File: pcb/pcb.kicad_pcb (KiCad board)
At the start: 2 copper layers, 130.9 x 223.4 mm, 38 parts, among them J1 Conn_01x04_Pin, J2 Conn_01x06_Pin, U1 XIAO-ESP32-C5-DIP, U10 XIAO-ESP32-C5-DIP, U11 XIAO-ESP32-C5-DIP, U12 XIAO-ESP32-C5-DIP, U13 XIAO-ESP32-C5-DIP, U14 XIAO-ESP32-C5-DIP, U15 XIAO-ESP32-C5-DIP, U18 XIAO-ESP32-C5-DIP, U19 LD1117V33, U2 XIAO-ESP32-C5-DIP, U3 XIAO-ESP32-C5-DIP, U4 XIAO-ESP32-C5-DIP, U5 XIAO-ESP32-C5-DIP, U6 XIAO-ESP32-C5-DIP, U7 XIAO-ESP32-C5-DIP, U8 XIAO-ESP32-C5-DIP, U9 XIAO-ESP32-C5-DIP

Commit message: add capacitors to i/o of LD1117
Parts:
- added C1: 100nF, Capacitor_THT:C_Disc_D5.0mm_W2.5mm_P2.50mm, F.Cu at (59.5, 23.0)
- added C2: 10uF, Capacitor_THT:C_Disc_D5.0mm_W2.5mm_P2.50mm, F.Cu at (75.0, 32.0)
- moved U19 7.52 mm to (66.5, 35.1)
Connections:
- U19 pad 2: Net-(J2-Pin_6) -> Net-(U19-VO)
- U19 pad 3: +5V -> Net-(U19-VI)

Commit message: Added net classes and colors, squared away controller footprint, sorted power input battery symbol
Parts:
- U17: renamed from U16; value ~ -> ESP32-S3 DevKitC-1
- renumbered U18 to U15, U15 to U16, U19 to U18
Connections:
- net Net-(U1-GPIO25_D2) renamed /CS 1
- net Net-(U10-GPIO25_D2) renamed /CS 10
- net Net-(U11-GPIO25_D2) renamed /CS 11
- net Net-(U12-GPIO25_D2) renamed /CS 12
- net Net-(U13-GPIO25_D2) renamed /CS 13
- net Net-(U14-GPIO25_D2) renamed /CS 14
- net Net-(U15-GPIO25_D2) renamed /CS 16
- net Net-(U16-GPIO14) renamed /CS 15
- net Net-(U16-GPIO15) renamed /CS 5
- net Net-(U16-GPIO18) renamed /CS 6
- net Net-(U16-GPIO2) renamed /CS 9
- net Net-(U16-GPIO5) renamed /CS 2
- net Net-(U16-GPIO6) renamed /CS 3
- net Net-(U16-GPIO7) renamed /CS 4
- net Net-(U16-GPIO8) renamed /CS 7
- net Net-(U16-GPIO9) renamed /CS 8

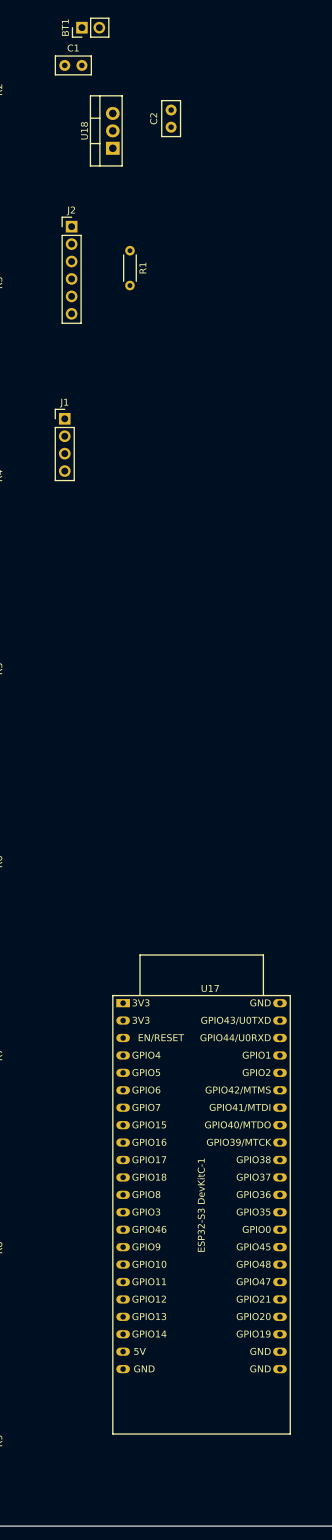
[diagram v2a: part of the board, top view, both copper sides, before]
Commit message: Fix ERC warnings, place new components in PCB
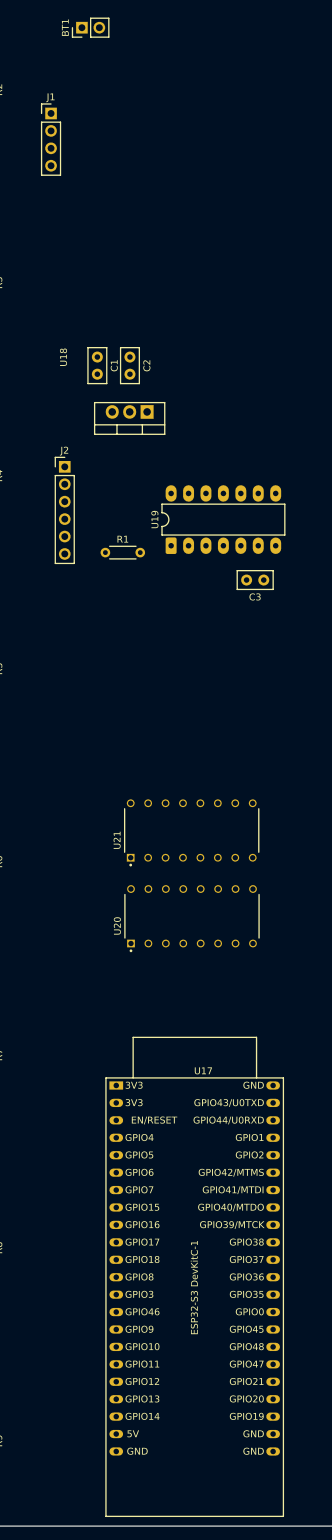
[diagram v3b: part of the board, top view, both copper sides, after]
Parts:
- added C3: 100nF, Capacitor_THT:C_Disc_D5.0mm_W2.5mm_P2.50mm, F.Cu at (88.5, 98.0)
- added U19: SN74HC125N, Package_DIP:DIP-14_W7.62mm_LongPads, F.Cu at (75.0, 93.0)
- added U20: SN74HC138N, SN74HC138N:DIP794W45P254L1969H508Q16, F.Cu at (78.0, 147.0)
- added U21: SN74HC138N, SN74HC138N:DIP794W45P254L1969H508Q16, F.Cu at (78.0, 134.5)
- J1: value Conn_01x04_Pin -> GPS Module Breakout
- J2: value Conn_01x06_Pin -> MicroSD Card Breakout
- moved J1 44.5 mm to (57.5, 30.0)
- moved R1 44.1 mm to (65.4, 94.0), turned to 0 degrees
- moved C1 42.8 mm to (64.2, 65.5), turned to -90 degrees
- moved U18 38.7 mm to (71.5, 73.5), turned to 180 degrees
- moved J2 35.0 mm to (59.5, 81.5)
- moved C2 34.0 mm to (69.0, 65.5), turned to -90 degrees
- moved U17 12.0 mm to (67.0, 171.7)
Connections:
- C1 pad 1: Net-(U18-VI) -> GND
- C2 pad 1: Net-(J2-Pin_6) -> /CS 00
- J2 pad 2: /SCK -> Net-(J2-Pin_2)
- J2 pad 3: /MOSI -> Net-(J2-Pin_3)
- J2 pad 4: /MISO -> Net-(J2-Pin_4)
- J2 pad 6: Net-(J2-Pin_6) -> /CS 00
- R1 pad 1: Net-(J2-Pin_1) -> /CS 00
- R1 pad 2: Net-(J2-Pin_6) -> /CS 00
- R10 pad 2: /CS 9 -> /CS 09
- R2 pad 2: /CS 1 -> /CS 01
- R3 pad 2: /CS 2 -> /CS 02
- R4 pad 2: /CS 3 -> /CS 03
- R5 pad 2: /CS 4 -> /CS 04
- R6 pad 2: /CS 5 -> /CS 05
- R7 pad 2: /CS 6 -> /CS 06
- R8 pad 2: /CS 7 -> /CS 07
- R9 pad 2: /CS 8 -> /CS 08
- U1 pad 3: /CS 1 -> /CS 01
- U17 pad 11: /CS 6 -> /CS ENABLE
- U17 pad 12: /CS 7 -> unconnected-(U17-GPIO8-Pad12)
- U17 pad 15: /CS 8 -> unconnected-(U17-GPIO9-Pad15)
- U17 pad 16: /CS 16 -> unconnected-(U17-GPIO10-Pad16)
- U17 pad 20: /CS 15 -> unconnected-(U17-GPIO14-Pad20)
- U17 pad 26: Net-(J2-Pin_1) -> unconnected-(U17-GPIO1-Pad26)
- U17 pad 27: /CS 9 -> unconnected-(U17-GPIO2-Pad27)
- U17 pad 28: /CS 10 -> unconnected-(U17-GPIO42-Pad28)
- U17 pad 29: /CS 11 -> unconnected-(U17-GPIO41-Pad29)
- U17 pad 30: /CS 12 -> unconnected-(U17-GPIO40-Pad30)
- U17 pad 31: /CS 13 -> unconnected-(U17-GPIO39-Pad31)
- U17 pad 4: /CS 1 -> /CS 00
- U17 pad 40: /CS 14 -> unconnected-(U17-GPIO21-Pad40)
- U17 pad 5: /CS 2 -> /CS Addr 1
- U17 pad 6: /CS 3 -> /CS Addr 2
- U17 pad 7: /CS 4 -> /CS Addr 3
- U17 pad 8: /CS 5 -> /CS Bank Sel
- U18 pad 3: Net-(U18-VI) -> +5V
- U2 pad 3: /CS 2 -> /CS 02
- U3 pad 3: /CS 3 -> /CS 03
- U4 pad 3: /CS 4 -> /CS 04
- U5 pad 3: /CS 5 -> /CS 05
- U6 pad 3: /CS 6 -> /CS 06
- U7 pad 3: /CS 7 -> /CS 07
- U8 pad 3: /CS 8 -> /CS 08
- U9 pad 3: /CS 9 -> /CS 09

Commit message: tidy up
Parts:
- moved J1 35.5 mm to (58.0, 65.5)
- moved C2 32.2 mm to (73.8, 97.4), turned to 180 degrees
- moved R1 28.6 mm to (63.0, 122.5)
- moved C3 21.8 mm to (92.5, 119.4)
- moved J2 21.4 mm to (58.5, 102.9)
- moved U19 19.9 mm to (72.4, 112.7)
- moved C1 17.4 mm to (68.5, 82.4)
- moved U18 16.6 mm to (73.5, 90.0)
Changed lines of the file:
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@@
 	(footprint "Package_DIP:DIP-14_W7.62mm_LongPads"
 		(layer "F.Cu")
-		(at 75 93 90)
+		(at 72.38 112.69 90)
 		(descr "14-lead though-hole mounted DIP package, row spacing 7.62mm (300 mils), LongPads")
 		(tags "THT DIP DIL PDIP 2.54mm 7.62mm 300mil LongPads")
@@
 		)
 		(point
-			(at 82.62 89.19)
+			(at 80 108.88)
 			(size 1.27)
 			(layer "F.Fab")
@@
 	(footprint "Capacitor_THT:C_Disc_D5.0mm_W2.5mm_P2.50mm"
 		(layer "F.Cu")
-		(at 69 65.5 -90)
+		(at 73.75 97.38 180)
 		(descr "C, Disc series, Radial, pin pitch=2.50mm, diameter*width=5*2.5mm^2, Capacitor, http://cdn-reichelt.de/documents/datenblatt/B300/DS_KERKO_TC.pdf")
 		(tags "C Disc series Radial pin pitch 2.50mm diameter 5mm width 2.5mm Capacitor")
 		(property "Reference" "C2"
-			(at 1.25 -2.5 90)
+			(at 1.25 -2.5 0)
 			(layer "F.SilkS")
 			(effects
@@
 		)
 		(property "Value" "10uF"
-			(at 1.25 2.5 90)
+			(at 1.25 2.5 0)
 			(layer "F.Fab")
 			(effects
@@
 		)
 		(property "Datasheet" ""
-			(at 0 0 90)
+			(at 0 0 0)
 			(layer "F.Fab")
 			(hide yes)
@@
 		)
 		(property "Description" "Unpolarized capacitor"
-			(at 0 0 90)
+			(at 0 0 0)
 			(layer "F.Fab")
 			(hide yes)
@@
 		)
 		(property "KiLib_Generator" "capacitor/THT/other"
-			(at 0 0 90)
+			(at 0 0 0)
 			(layer "F.SilkS")
 			(hide yes)
@@
 		(duplicate_pad_numbers_are_jumpers no)
 		(fp_line
-			(start -1.37 1.37)
-			(end -1.37 -1.37)
+			(start 3.87 1.37)
+			(end -1.37 1.37)
 			(stroke
 				(width 0.12)
@@
 		)
 		(fp_line
-			(start 3.87 1.37)
-			(end -1.37 1.37)
+			(start 3.87 -1.37)
+			(end 3.87 1.37)
 			(stroke
 				(width 0.12)
@@
 		)
 		(fp_line
-			(start -1.37 -1.37)
-			(end 3.87 -1.37)
+			(start -1.37 1.37)
+			(end -1.37 -1.37)
 			(stroke
 				(width 0.12)
@@
 		)
 		(fp_line
-			(start 3.87 -1.37)
-			(end 3.87 1.37)
+			(start -1.37 -1.37)
+			(end 3.87 -1.37)
 			(stroke
 				(width 0.12)
@@
 		)
 		(fp_text user "${REFERENCE}"
-			(at 1.25 0 90)
+			(at 1.25 0 0)
 			(layer "F.Fab")
 			(effects
@@
 		)
 		(pad "1" thru_hole circle
-			(at 0 0 270)
+			(at 0 0 180)
 			(size 1.6 1.6)
 			(drill 0.8)
@@
 		)
 		(pad "2" thru_hole circle
-			(at 2.5 0 270)
+			(at 2.5 0 180)
 			(size 1.6 1.6)
 			(drill 0.8)
@@
 	(footprint "Capacitor_THT:C_Disc_D5.0mm_W2.5mm_P2.50mm"
 		(layer "F.Cu")
-		(at 64.25 65.5 -90)
+		(at 68.5 82.38 -90)
 		(descr "C, Disc series, Radial, pin pitch=2.50mm, diameter*width=5*2.5mm^2, Capacitor, http://cdn-reichelt.de/documents/datenblatt/B300/DS_KERKO_TC.pdf")
 		(tags "C Disc series Radial pin pitch 2.50mm diameter 5mm width 2.5mm Capacitor")
@@
 	(footprint "Package_TO_SOT_THT:TO-220-3_Vertical"
 		(layer "F.Cu")
-		(at 71.5 73.5 180)
+		(at 73.5 90 180)
 		(descr "TO-220-3, Vertical, RM 2.54mm, see https://www.vishay.com/docs/66542/to-220-1.pdf")
 		(tags "TO-220-3 Vertical RM 2.54mm")
 		(property "Reference" "U18"
-			(at 12.15 7.96 90)
+			(at 9 -1 90)
 			(layer "F.SilkS")
 			(effects
@@
 	(footprint "Resistor_THT:R_Axial_DIN0204_L3.6mm_D1.6mm_P5.08mm_Horizontal"
 		(layer "F.Cu")
-		(at 65.42 94)
+		(at 63 122.5)
 		(descr "Resistor, Axial_DIN0204 series, Axial, Horizontal, pin pitch=5.08mm, 0.167W, length*diameter=3.6*1.6mm^2, http://cdn-reichelt.de/documents/datenblatt/B400/1_4W%23YAG.pdf")
 		(tags "Resistor Axial_DIN0204 series Axial Horizontal pin pitch 5.08mm 0.167W length 3.6mm diameter 1.6mm")
@@
 		)
 		(property "Value" "SN74HC138N"
-			(at 11.275 10.835 90)
+			(at 0.5 11.96 90)
 			(layer "F.Fab")
 			(effects
@@
 	(footprint "Connector_PinHeader_2.54mm:PinHeader_1x06_P2.54mm_Vertical"
 		(layer "F.Cu")
-		(at 59.5 81.5)
+		(at 58.5 102.88)
 		(descr "Through hole straight pin header, 1x06, 2.54mm pitch, single row")
 		(tags "Through hole pin header THT 1x06 2.54mm single row")
@@
 	(footprint "Capacitor_THT:C_Disc_D5.0mm_W2.5mm_P2.50mm"
 		(layer "F.Cu")
-		(at 88.5 98 180)
+		(at 92.5 119.38 180)
 		(descr "C, Disc series, Radial, pin pitch=2.50mm, diameter*width=5*2.5mm^2, Capacitor, http://cdn-reichelt.de/documents/datenblatt/B300/DS_KERKO_TC.pdf")
 		(tags "C Disc series Radial pin pitch 2.50mm diameter 5mm width 2.5mm Capacitor")
@@
 		)
 		(property "Value" "SN74HC138N"
-			(at 11.275 10.835 90)
+			(at 0 12 90)
 			(layer "F.Fab")
 			(effects
@@
 	(footprint "Connector_PinHeader_2.54mm:PinHeader_1x04_P2.54mm_Vertical"
 		(layer "F.Cu")
-		(at 57.5 30)
+		(at 58 65.46)
 		(descr "Through hole straight pin header, 1x04, 2.54mm pitch, single row")
 		(tags "Through hole pin header THT 1x04 2.54mm single row")
